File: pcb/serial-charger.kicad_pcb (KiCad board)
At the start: 2 copper layers, 87 x 21 mm, 73 parts, among them IC1 CH340G, IC2 ATMEGA168-P, J1 jumper, J2 jumper, P1 CONN_01X02, P10 CONNECTOR, P11 CONNECTOR, P12 CONNECTOR, P13 CONNECTOR, P14 CONNECTOR, P15 CONNECTOR, P16 CONNECTOR, P17 CONNECTOR, P18 CONNECTOR, P19 CONNECTOR, P2 USB_OTG, P20 CONNECTOR, P21 CONNECTOR, P22 CONNECTOR, P23 CONNECTOR, P24 CONNECTOR, P25 CONN_01X03, P3 CONN_01X04, P4 CONNECTOR, P5 CONNECTOR, P6 CONNECTOR, P7 CONNECTOR, P8 CONNECTOR, P9 CONNECTOR, U1 XC6206, U2 FM6316FE, x1 xtal_osc, x2 xtal_osc

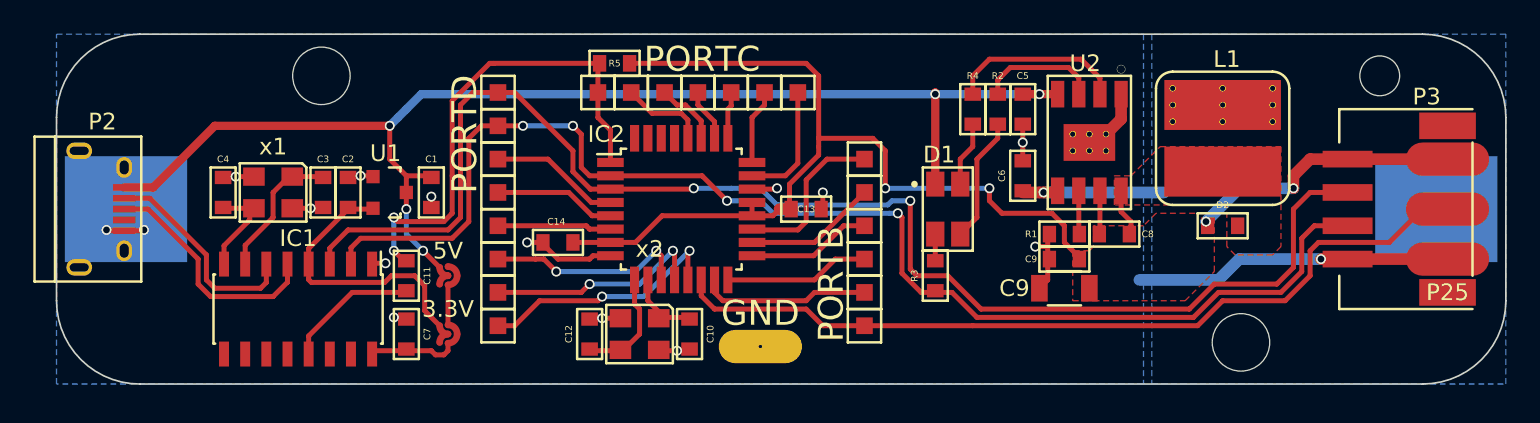
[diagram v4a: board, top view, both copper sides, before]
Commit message: changed mcu to the correct one. redid layout
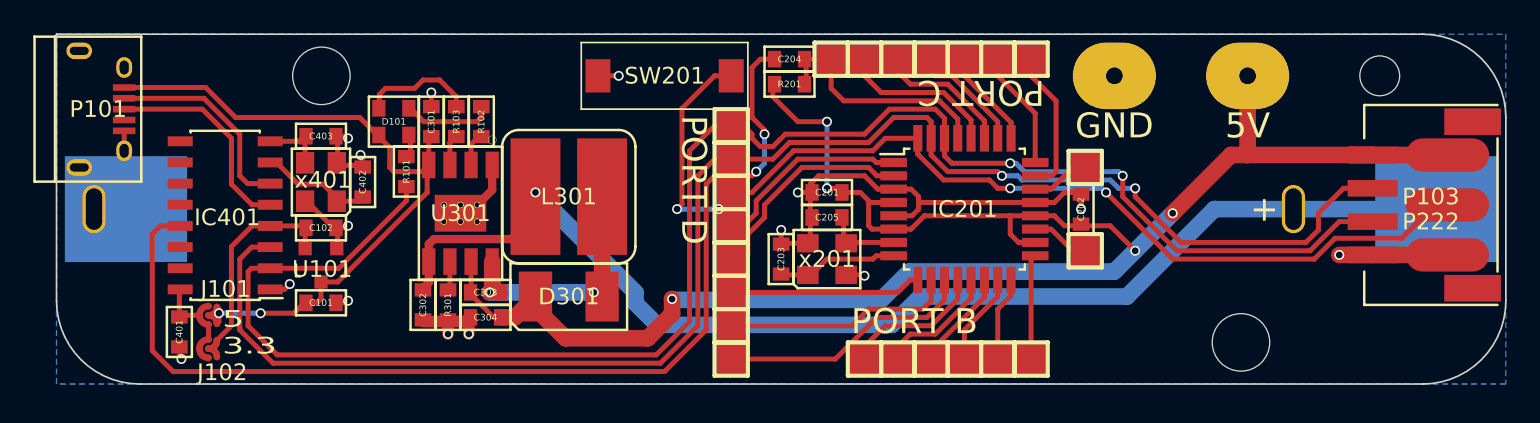
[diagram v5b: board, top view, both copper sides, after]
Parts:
- removed C1, C2, C5, C6, C7: 10u, netl:SMD_0603
- removed C10, C11, C12, C13, C14, C8: C, netl:SMD_0603
- removed C3, C4: 22p, netl:SMD_0603
- removed C9: 47uF, Capacitors_SMD:C_1206
- removed C9: 47uF, netl:SMD_0603
- removed D1: RGB_LED, netl:RGB_LED
- removed D2: D, netl:SMD_0603
- removed G***: LOGO, netl:LOGO_127mm_Bottom_SS
- removed IC1: CH340G, Housings_SOIC:SOIC-16_3.9x9.9mm_Pitch1.27mm
- removed IC2: ATMEGA168-P, Housings_QFP:TQFP-32_7x7mm_Pitch0.8mm
- removed J1, J2: jumper, netl:Jumper
- removed L1: INDUCTOR, netl:7x7_Inductor
- removed P1: CONN_01X02, netl:18560
- removed P10, P11, P12, P13, P14, P15, P16, P17, P18, P19, P20, P21, P22, P23, P24, P4, P5, P6, P7, P8, P9: CONNECTOR, netl:1Pin_small
- removed P2: USB_OTG, Connect:USB_Micro-B
- removed P25: CONN_01X03, netl:SM_3_WIRE
- removed P3: CONN_01X04, netl:JST-2mm_4Pin
- removed R1: 2k, netl:SMD_0603
- removed R2, R3, R4: 1k, netl:SMD_0603
- removed R5: R, netl:SMD_0603
- removed the REF** at (173.5, 94.8)
- removed the REF** at (169.5, 95.5)
- removed the REF** at (168.5, 95.5)
- removed the REF** at (168.5, 96.5)
- removed the REF** at (169.5, 96.5)
- removed the REF** at (167.5, 96.5)
- removed the REF** at (167.5, 95.5)
- removed the REF** at (148.8, 108.2)
- removed the REF** at (173.5, 93.8)
- removed the REF** at (173.5, 92.8)
- removed the REF** at (176.5, 92.8)
- removed the REF** at (176.5, 93.8)
- removed the REF** at (176.5, 94.8)
- removed the REF** at (179.5, 93.8)
- removed the REF** at (179.5, 94.8)
- removed the REF** at (179.5, 92.8)
- removed U1: XC6206, TO_SOT_Packages_SMD:SOT-23
- removed U2: FM6316FE, netl:ESOP-8
- removed x1, x2: xtal_osc, netl:SM_3225
- added C101: 10u, netl:SMD_0603, F.Cu at (122.4, 105.6)
- added C102: 10u, netl:SMD_0603, F.Cu at (122.4, 101.1)
- added C201: C, netl:SMD_0603, F.Cu at (152.8, 99.0)
- added C202: C, netl:SMD_0603, F.Cu at (168.0, 100.0)
- added C203: C, netl:SMD_0603, F.Cu at (150.0, 103.0)
- added C204: C, netl:SMD_0603, F.Cu at (150.5, 91.0)
- added C205: C, netl:SMD_0603, F.Cu at (152.8, 100.5)
- added C301: 10u, netl:SMD_0603, F.Cu at (129.0, 94.8)
- added C302: 10uF, netl:SMD_0603, F.Cu at (128.5, 105.8)
- added C303: 2nF, netl:SMD_0603, F.Cu at (132.2, 105.0)
- added C304: 47uF, netl:SMD_0603, F.Cu at (132.2, 106.5)
- added C401: 10u, netl:SMD_0603, F.Cu at (113.9, 107.4)
- added C402: 22p, netl:SMD_0603, F.Cu at (124.9, 98.4)
- added C403: 22p, netl:SMD_0603, F.Cu at (122.4, 95.6)
- added D101: RGB_LED, netl:SMD_0606, F.Cu at (126.8, 94.8)
- added D301: D, netl:DO-214AC, F.Cu at (137.2, 105.2)
- added IC201: ATMEGA328P-M, Housings_QFP:TQFP-32_7x7mm_Pitch0.8mm, F.Cu at (161.0, 100.0)
- added IC401: CH340G, Housings_SOIC:SOIC-16_3.9x9.9mm_Pitch1.27mm, F.Cu at (116.6, 100.4)
- added J101: jumper, netl:Jumper, F.Cu at (115.6, 106.4)
- added J102: jumper, netl:Jumper, F.Cu at (115.6, 108.4)
- added L301: 3.3uH, netl:7x7_Inductor, F.Cu at (137.2, 99.2)
- added P101: USB_OTG, Connect:USB_Micro-B, F.Cu at (109.0, 94.0)
- added P102: CONN_01X02, netl:18560, B.Cu at (150.0, 100.0)
- added P103: CONN_01X04, netl:JST-2mm_4Pin, F.Cu at (189.0, 99.8)
- added P201: CONNECTOR, netl:1Pin_big, F.Cu at (155.0, 109.0)
- added P202: CONNECTOR, netl:1Pin_big, F.Cu at (157.0, 109.0)
- added P203: CONNECTOR, netl:1Pin_big, F.Cu at (159.0, 109.0)
- added P204: CONNECTOR, netl:1Pin_big, F.Cu at (161.0, 109.0)
- added P205: CONNECTOR, netl:1Pin_big, F.Cu at (163.0, 109.0)
- added P206: CONNECTOR, netl:1Pin_big, F.Cu at (165.0, 109.0)
- added P207: CONNECTOR, netl:1Pin_big, F.Cu at (165.0, 91.0)
- added P208: CONNECTOR, netl:1Pin_big, F.Cu at (163.0, 91.0)
- added P209: CONNECTOR, netl:1Pin_big, F.Cu at (161.0, 91.0)
- added P210: CONNECTOR, netl:1Pin_big, F.Cu at (159.0, 91.0)
- added P211: CONNECTOR, netl:1Pin_big, F.Cu at (157.0, 91.0)
- added P212: CONNECTOR, netl:1Pin_big, F.Cu at (155.0, 91.0)
- added P213: CONNECTOR, netl:1Pin_big, F.Cu at (153.0, 91.0)
- added P214: CONNECTOR, netl:1Pin_big, F.Cu at (147.0, 95.0)
- added P215: CONNECTOR, netl:1Pin_big, F.Cu at (147.0, 97.0)
- added P216: CONNECTOR, netl:1Pin_big, F.Cu at (147.0, 99.0)
- added P217: CONNECTOR, netl:1Pin_big, F.Cu at (147.0, 101.0)
- added P218: CONNECTOR, netl:1Pin_big, F.Cu at (147.0, 103.0)
- added P219: CONNECTOR, netl:1Pin_big, F.Cu at (147.0, 105.0)
- added P220: CONNECTOR, netl:1Pin_big, F.Cu at (147.0, 107.0)
- added P221: CONNECTOR, netl:1Pin_big, F.Cu at (147.0, 109.0)
- added P222: CONN_01X03, netl:SM_3_WIRE, F.Cu at (190.0, 99.8)
- added P223: CONNECTOR, netl:1Pin_big, F.Cu at (168.2, 102.5)
- added P224: CONNECTOR, netl:1Pin_big, F.Cu at (168.2, 97.5)
- added R101: 1k, netl:SMD_0603, F.Cu at (127.5, 97.8)
- added R102: 1k, netl:SMD_0603, F.Cu at (132.0, 94.8)
- added R103: 1k, netl:SMD_0603, F.Cu at (130.5, 94.8)
- added R201: R, netl:SMD_0603, F.Cu at (150.5, 92.5)
- added R301: 2k, netl:SMD_0603, F.Cu at (130.0, 105.8)
- added REF**: via, netl:via, F.Cu at (170.0, 92.0)
- added REF**: via, netl:via, F.Cu at (178.0, 92.0)
- added REF**: via, netl:via, F.Cu at (180.8, 100.0)
- added REF**: via, netl:via, F.Cu at (129.8, 99.8)
- added REF**: via, netl:via, F.Cu at (130.8, 99.8)
- added REF**: via, netl:via, F.Cu at (131.8, 99.8)
- added REF**: via, netl:via, F.Cu at (131.8, 100.8)
- added REF**: via, netl:via, F.Cu at (130.8, 100.8)
- added REF**: via, netl:via, F.Cu at (129.8, 100.8)
- added REF**: via, netl:via, F.Cu at (108.8, 100.0)
- added SW201: SW_PUSH, netl:Button, F.Cu at (143.0, 92.0)
- added U101: XC6206, TO_SOT_Packages_SMD:SOT-23, F.Cu at (122.4, 103.4)
- added U301: FM6316FE, netl:ESOP-8, F.Cu at (130.8, 100.2)
- added x201: xtal_osc, netl:SM_3225, F.Cu at (152.8, 103.0)
- added x401: xtal_osc, netl:SM_3225, F.Cu at (122.4, 98.4)
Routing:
- net /Battery Management/5V_OUT: track 0.00 -> 109.9 mm, vias 0 -> 5
- net /avr/RX: track 0.00 -> 103.1 mm, vias 0 -> 2
- net /USB to Serial/RX: track 0.00 -> 93.2 mm, vias 0 -> 2
- net RX: track 83.6 -> 0.00 mm, vias 2 -> 0
- net TX: track 78.4 -> 0.00 mm, vias 4 -> 0
- net /Battery Management/V_BAT: track 0.00 -> 76.5 mm, vias 0 -> 1
- net V_USB: track 76.2 -> 0.00 mm, vias 5 -> 0
- net 5V: track 76.1 -> 0.00 mm, vias 4 -> 0
- net /USB to Serial/~DTR: track 0.00 -> 64.0 mm, vias 0 -> 2
- net /Battery Management/5V_IN: track 0.00 -> 42.7 mm, vias 0 -> 2
- net /avr/btn: track 0.00 -> 26.2 mm, vias 0 -> 2
- net Net-(C303-Pad2): track 0.00 -> 17.6 mm, vias 0 -> 2
- net 3V3: track 17.0 -> 0.00 mm
- net Net-(IC201-Pad11): track 0.00 -> 15.5 mm
- net /avr/~RESET: track 29.7 -> 14.3 mm, vias 2 -> 0
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- removed copper zone on F.Cu, net 5V
- removed copper zone on F.Cu, net Net-(C8-Pad2)
- removed copper zone on B.Cu, net VBat
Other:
- outline, holes or cut-outs redrawn
- board text added: "+"
- board text added: "-"
- board text added: "5 3.3"
- board text added: "PORT B"
- board text added: "PORT C"
- board text added: "PORT D"
- board text added: "party hat driver Revision 39427861509658702384708 "final prototype""
- board text removed: "3.3V"
- board text removed: "Hi there!"
- board text removed: "PORTB"
- board text removed: "PORTC"
- board text removed: "PORTD"

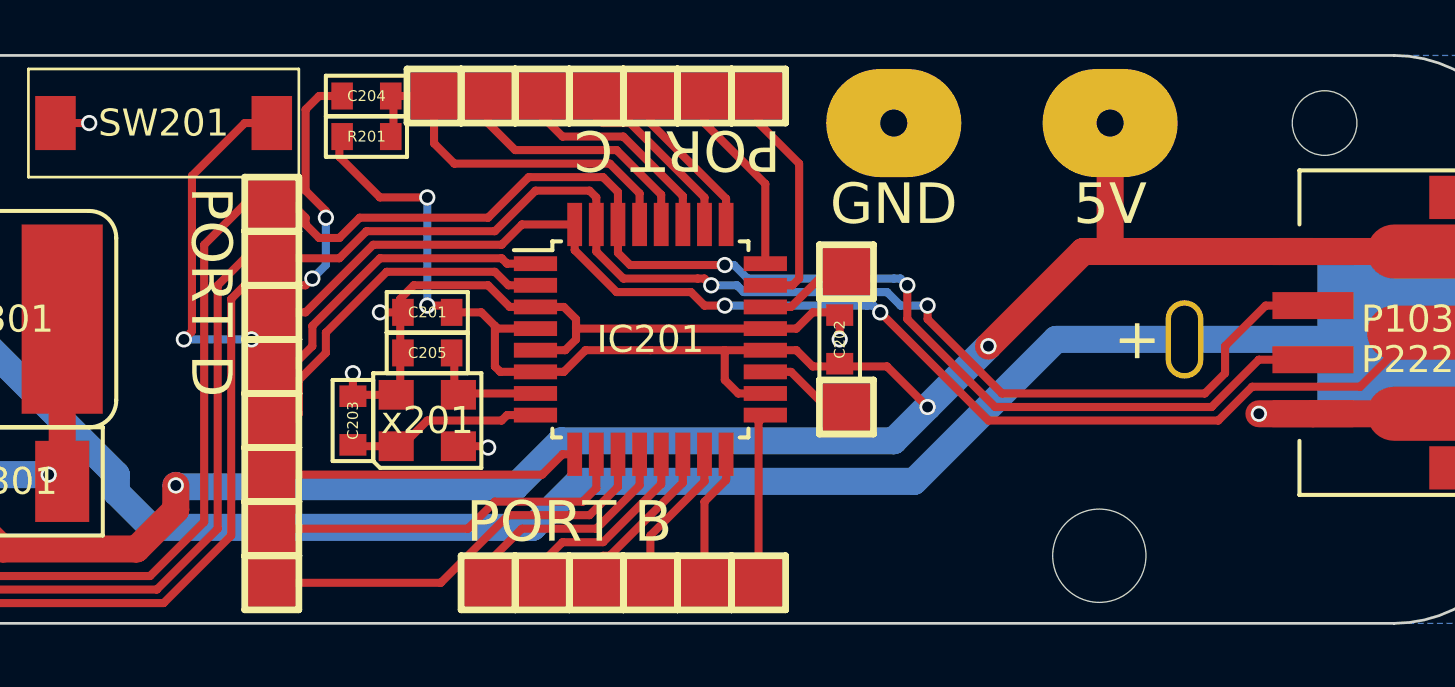
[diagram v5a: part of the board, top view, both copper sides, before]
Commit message: fixed short circuits caused by oversized breakout pads
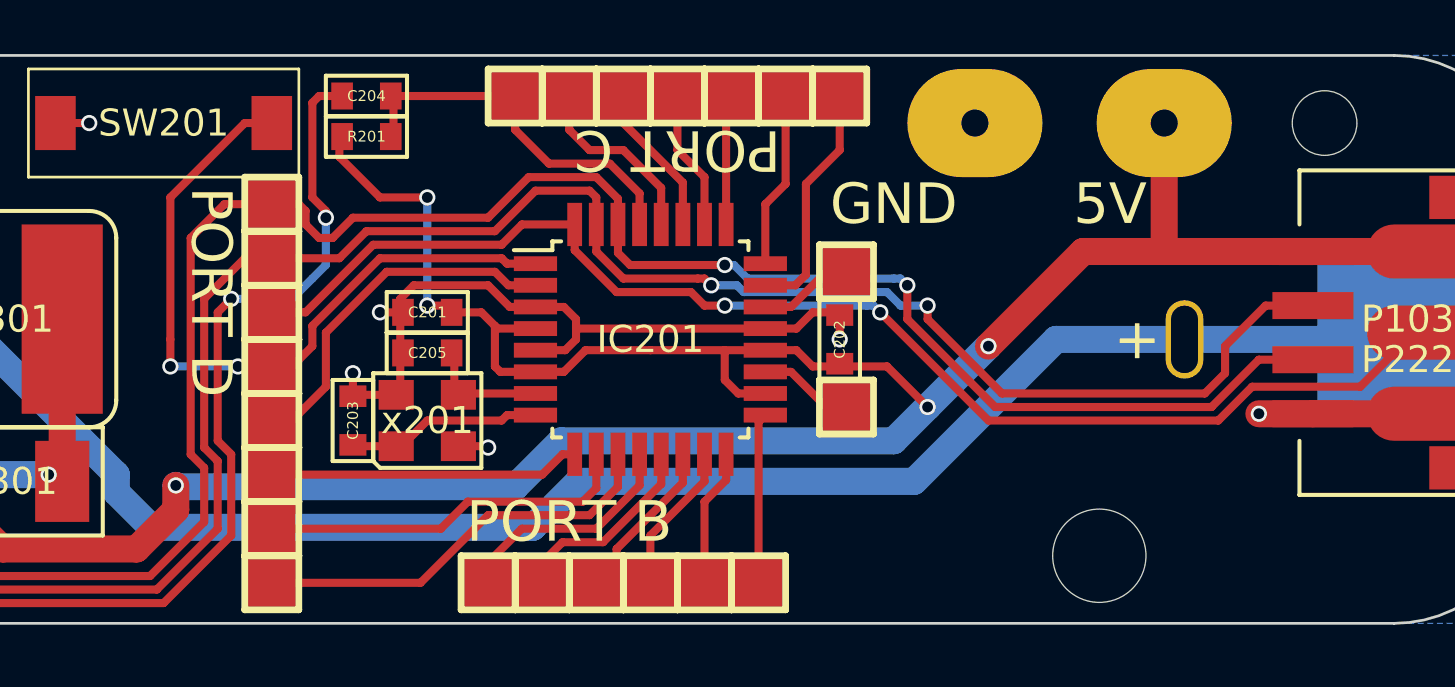
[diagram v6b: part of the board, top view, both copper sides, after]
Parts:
- moved P207 3.00 mm to (168.0, 91.0)
- moved P208 3.00 mm to (166.0, 91.0)
- moved P209 3.00 mm to (164.0, 91.0)
- moved P210 3.00 mm to (162.0, 91.0)
- moved P211 3.00 mm to (160.0, 91.0)
- moved P212 3.00 mm to (158.0, 91.0)
- moved P213 3.00 mm to (156.0, 91.0)
- moved REF** 3.00 mm to (173.0, 92.0)
- moved REF** 2.00 mm to (180.0, 92.0)
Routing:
- net Net-(IC201-Pad28): track 9.60 -> 6.89 mm
- net Net-(IC201-Pad27): track 8.22 -> 6.41 mm
- net Net-(IC201-Pad26): track 6.99 -> 5.91 mm
- net Net-(IC201-Pad25): track 5.91 -> 4.83 mm
- net /avr/RX: track 103.1 -> 103.9 mm
- net /avr/btn: track 26.2 -> 27.1 mm
- net Net-(IC201-Pad24): track 7.13 -> 6.51 mm

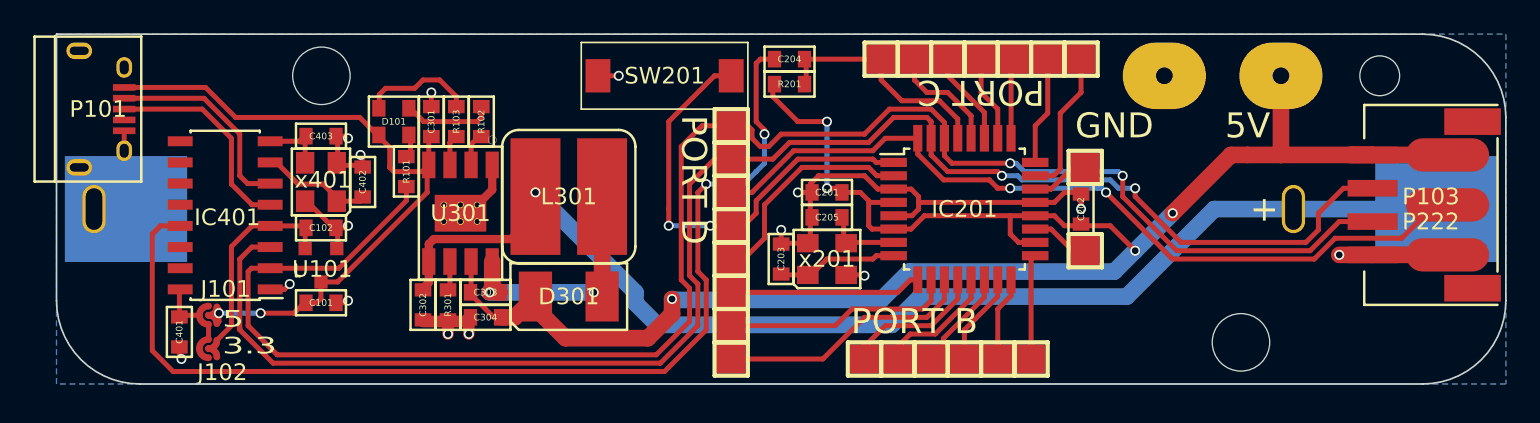
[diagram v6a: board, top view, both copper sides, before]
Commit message: centered battery tab connectors, reworked layout to match it
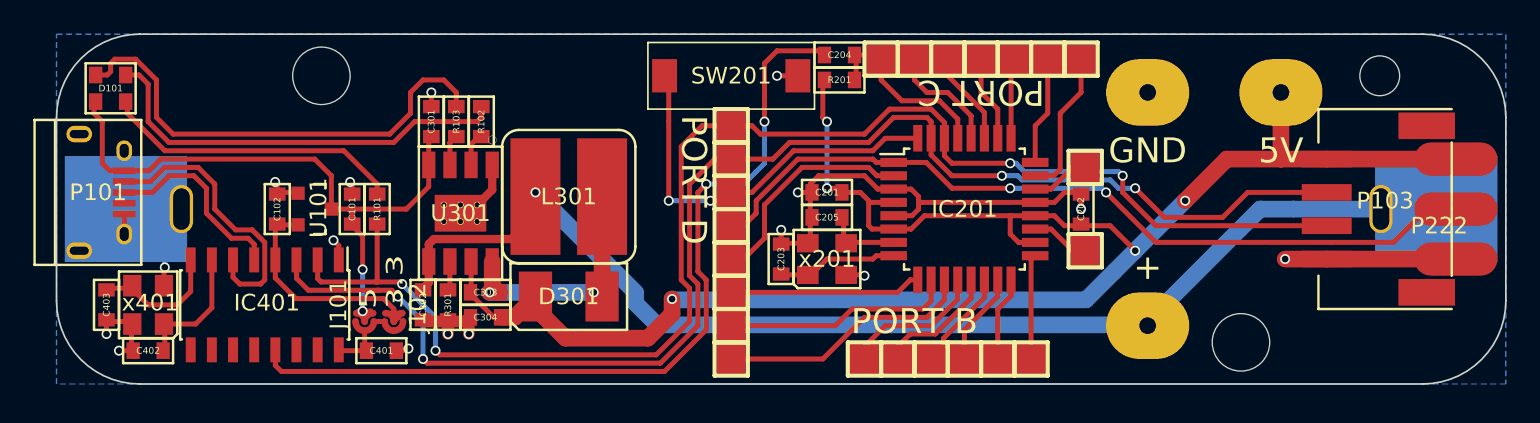
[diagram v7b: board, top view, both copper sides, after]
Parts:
- added REF**: via, netl:via, F.Cu at (172.0, 107.0)
- C201, C202, C204: value C -> 100n
- C203, C205: value C -> 22p
- R201: value R -> 10k
- moved D101 17.1 mm to (109.8, 92.8)
- moved C402 16.4 mm to (112.0, 108.5), turned to 180 degrees
- moved C403 16.4 mm to (109.5, 105.8), turned to 270 degrees
- moved x401 12.7 mm to (112.0, 105.8)
- moved C401 12.2 mm to (126.0, 108.5), turned to 180 degrees
- moved J102 11.2 mm to (126.8, 106.8), turned to 270 degrees
- moved J101 9.38 mm to (125.0, 106.8), turned to 270 degrees
- moved C101 5.93 mm to (124.2, 100.0), turned to 90 degrees
- moved IC401 5.88 mm to (119.0, 105.8), turned to 270 degrees
- moved REF** 5.25 mm to (114.0, 100.0)
- moved REF** 5.25 mm to (186.0, 100.0)
- moved P101 5.00 mm to (109.0, 99.0)
- moved SW201 4.00 mm to (147.0, 92.0), turned to 0 degrees
- moved U101 3.40 mm to (122.0, 100.0), turned to 270 degrees
- moved C204 3.01 mm to (153.5, 90.8)
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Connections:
- IC201 pad 1: /avr/btn -> /avr/LED_SRIP
- IC201 pad 32: /avr/LED_SRIP -> /avr/BTN
- P216 pad 1: /avr/LED_SRIP -> /avr/BTN
- P217 pad 1: /avr/btn -> /avr/LED_SRIP
- SW201 pad 1: /avr/btn -> /avr/BTN
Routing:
- net /avr/btn: track 27.1 -> 0.00 mm, vias 2 -> 0
- net /avr/BTN: track 0.00 -> 24.1 mm, vias 0 -> 2
- net Net-(D101-Pad1): track 6.78 -> 28.8 mm
- net Net-(D101-Pad2): track 5.43 -> 25.6 mm
- net /avr/RX: track 103.9 -> 86.4 mm, vias 2 -> 4
- net Net-(D101-Pad3): track 1.30 -> 18.0 mm
- net /USB to Serial/~DTR: track 64.2 -> 51.1 mm
- net /USB to Serial/RX: track 93.6 -> 82.7 mm, vias 2 -> 4
- net GND: track 57.4 -> 64.6 mm, vias 15 -> 16
- net /USB to Serial/D-: track 12.3 -> 17.0 mm
- net /Battery Management/5V_IN: track 42.7 -> 38.5 mm
- net Net-(C403-Pad1): track 3.80 -> 7.94 mm
- net /Battery Management/5V_OUT: track 109.9 -> 106.3 mm
- net /avr/~RESET: track 14.0 -> 11.1 mm
- net Net-(C402-Pad1): track 6.69 -> 8.15 mm
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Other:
- outline, holes or cut-outs redrawn
- board text added: "Greets: hacklab.fi, nakkiservo, Elite Dekkerz"
- board text removed: "party hat driver Revision 39427861509658702384708 "final prototype""

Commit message: cleaned up component values, rebuilt BOM
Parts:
- C302: value 10uF -> 10u
- C303: value 2nF -> 2n
- C304: value 47uF -> 47u
- D301: value D -> 1N5822
- L301: value 3.3uH -> 3.3u
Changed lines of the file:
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@@
 (kicad_pcb (version 4) (host pcbnew 4.0.2+dfsg1-stable)
   (general
-    (links 130)
-    (no_connects 4)
+    (links 129)
+    (no_connects 5)
     (area 106.449999 89.449999 193.550001 110.550001)
     (thickness 1.6)
@@
   )
   (setup
-    (last_trace_width 1)
+    (last_trace_width 0.25)
     (user_trace_width 0.2)
     (user_trace_width 0.3)
@@
     (mod_text_size 1 1)
     (mod_text_width 0.15)
-    (pad_size 0.4 0.4)
-    (pad_drill 0.3)
+    (pad_size 2.21 3.1)
+    (pad_drill 0)
     (pad_to_mask_clearance 0)
     (aux_axis_origin 0 0)
@@
       (effects (font (size 0.4 0.4) (thickness 0.05)))
     )
-    (fp_text value 10uF (at 0 -0.8 270) (layer F.Fab)
+    (fp_text value 10u (at 0 -0.8 270) (layer F.Fab)
       (effects (font (size 0.4 0.4) (thickness 0.1)))
     )
@@
       (effects (font (size 0.4 0.4) (thickness 0.05)))
     )
-    (fp_text value 2nF (at 0 -0.8) (layer F.Fab)
+    (fp_text value 2n (at 0 -0.8) (layer F.Fab)
       (effects (font (size 0.4 0.4) (thickness 0.1)))
     )
@@
       (effects (font (size 0.4 0.4) (thickness 0.05)))
     )
-    (fp_text value 47uF (at 0 -0.8 180) (layer F.Fab)
+    (fp_text value 47u (at 0 -0.8 180) (layer F.Fab)
       (effects (font (size 0.4 0.4) (thickness 0.1)))
     )
@@
       (effects (font (size 1 1) (thickness 0.15)))
     )
-    (fp_text value D (at 0 -3) (layer F.Fab)
+    (fp_text value 1N5822 (at 0 -3) (layer F.Fab)
       (effects (font (size 1 1) (thickness 0.15)))
     )
@@
       (effects (font (size 1 1) (thickness 0.15)))
     )
-    (fp_text value 3.3uH (at 0 -5.08 90) (layer F.Fab)
+    (fp_text value 3.3u (at 0 -5.08 90) (layer F.Fab)
       (effects (font (size 1 1) (thickness 0.15)))
     )
@@
   (segment (start 144 100.5) (end 144 100.5) (width 0.3) (layer F.Cu) (net 0))
   (segment (start 149 100.5) (end 149 100.5) (width 0.3) (layer F.Cu) (net 0))
-  (segment (start 182.75 103) (end 180.25 103) (width 1) (layer F.Cu) (net 1) (status 400000))
+  (segment (start 182.75 103) (end 180.25 103) (width 1) (layer F.Cu) (net 1))
   (via (at 180.25 103) (size 0.6) (drill 0.4) (layers F.Cu B.Cu) (net 1))
   (segment (start 113 102.33) (end 113 103.5) (width 0.3) (layer B.Cu) (net 1))
@@
   (segment (start 149 91.25) (end 149.75 90.5) (width 0.3) (layer F.Cu) (net 9))
   (segment (start 152.25 90.5) (end 152.5 90.75) (width 0.3) (layer F.Cu) (net 9))
-  (segment (start 172 107) (end 172 106.75) (width 1) (layer B.Cu) (net 10) (status C00000))
-  (segment (start 172 106.75) (end 178.75 100) (width 1) (layer B.Cu) (net 10) (status 400000))
-  (segment (start 156.65 106.95) (end 171.95 106.95) (width 1) (layer B.Cu) (net 10) (status 800000))
-  (segment (start 171.95 106.95) (end 172 107) (width 1) (layer B.Cu) (net 10) (status C00000))
+  (segment (start 172 107) (end 172 106.75) (width 1) (layer B.Cu) (net 10))
+  (segment (start 172 106.75) (end 178.75 100) (width 1) (layer B.Cu) (net 10))
+  (segment (start 156.65 106.95) (end 171.95 106.95) (width 1) (layer B.Cu) (net 10))
+  (segment (start 171.95 106.95) (end 172 107) (width 1) (layer B.Cu) (net 10))
   (segment (start 180.75 100) (end 189.33 100) (width 1) (layer B.Cu) (net 10))
   (segment (start 180.75 100) (end 178.75 100) (width 1) (layer B.Cu) (net 10))
